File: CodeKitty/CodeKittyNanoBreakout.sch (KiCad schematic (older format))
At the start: 17 parts, among them P1 CONN_01X02, P2 CONN_01X02, P3 CONN_01X03, P4 CONN_01X03, P5 CONN_01X03, Q1 MMBT3904, SW1 SW_PUSH_SMALL_H, SW2 Switch_SPDT_x2, U1 ArduinoNano

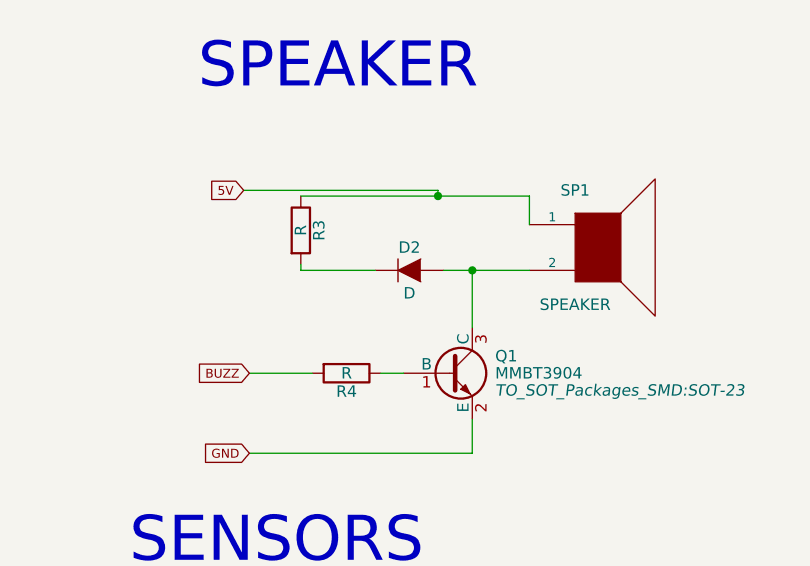
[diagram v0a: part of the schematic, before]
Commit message: fixed CKN
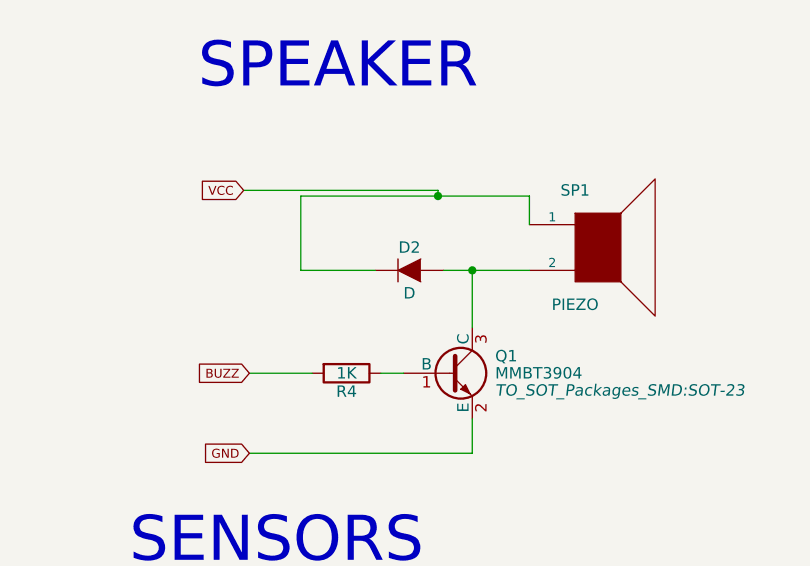
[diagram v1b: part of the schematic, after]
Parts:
- removed R3: R, Resistors_SMD:R_0603_HandSoldering, symbol R
- R4: value R -> 1K
- SP1: value SPEAKER -> PIEZO
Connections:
- net 5V: no longer SP1.1
- net VCC: now also D2.1 (K), SP1.1
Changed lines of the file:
@@
 P 9975 1550
 F 0 "SP1" H 9875 1800 50  0000 C CNN
-F 1 "SPEAKER" H 9875 1300 50  0000 C CNN
+F 1 "PIEZO" H 9875 1300 50  0000 C CNN
 F 2 "DM_Custom:DM_PiezSMD_PMKCS0909E4000-R1" H 9975 1550 50  0001 C CNN
 F 3 "" H 9975 1550 50  0000 C CNN
@@
 SENSORS
 Text GLabel 8425 1300 0    39   Input ~ 0
-5V
+VCC
 $Comp
 L D D2
@@
 $EndComp
 $Comp
-L R R3
-U 1 1 5A0CCF8E
-P 8675 1475
-F 0 "R3" V 8755 1475 50  0000 C CNN
-F 1 "R" V 8675 1475 50  0000 C CNN
-F 2 "Resistors_SMD:R_0603_HandSoldering" V 8605 1475 50  0001 C CNN
-F 3 "" H 8675 1475 50  0000 C CNN
-	1    8675 1475
-	1    0    0    -1
-$EndComp
-$Comp
 L R R4
 U 1 1 5A0CD00D
 P 8875 2100
 F 0 "R4" V 8955 2100 50  0000 C CNN
-F 1 "R" V 8875 2100 50  0000 C CNN
+F 1 "1K" V 8875 2100 50  0000 C CNN
 F 2 "Resistors_SMD:R_0603_HandSoldering" V 8805 2100 50  0001 C CNN
 F 3 "" H 8875 2100 50  0000 C CNN
@@
 Connection ~ 9425 1650
 Wire Wire Line
-	9000 1650 8675 1650
+	8675 1650 9000 1650
 Wire Wire Line
-	8675 1650 8675 1625
+	8675 1325 8675 1650
 Wire Wire Line
 	8675 1325 9675 1325
